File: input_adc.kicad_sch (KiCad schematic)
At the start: 8 parts

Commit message: Init Documentación
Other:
- note added: "Etapa: Entradas analógias"
- note added: "Pines ESP32/Input ADC - IA07 - IA08"
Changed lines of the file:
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@@
     (stroke (width 0) (type default) (color 0 0 0 0))
+  )
+  (text "Etapa: Entradas analógias" (at 99.06 45.72 0)
+    (effects (font (size 5.08 5.08) (thickness 1.016) bold) (justify left bottom))
+  )
+  (text "Pines ESP32/Input ADC\n\n- IA07\n- IA08\n\n\n" (at 60.96 157.48 0)
+    (effects (font (size 2.54 2.54)) (justify left bottom))
   )
   (global_label "IA08" (shape input) (at 120.65 105.41 180) (fields_autoplaced)

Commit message: update esq raiz
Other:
- moved on the sheet: C?, R?, U?B

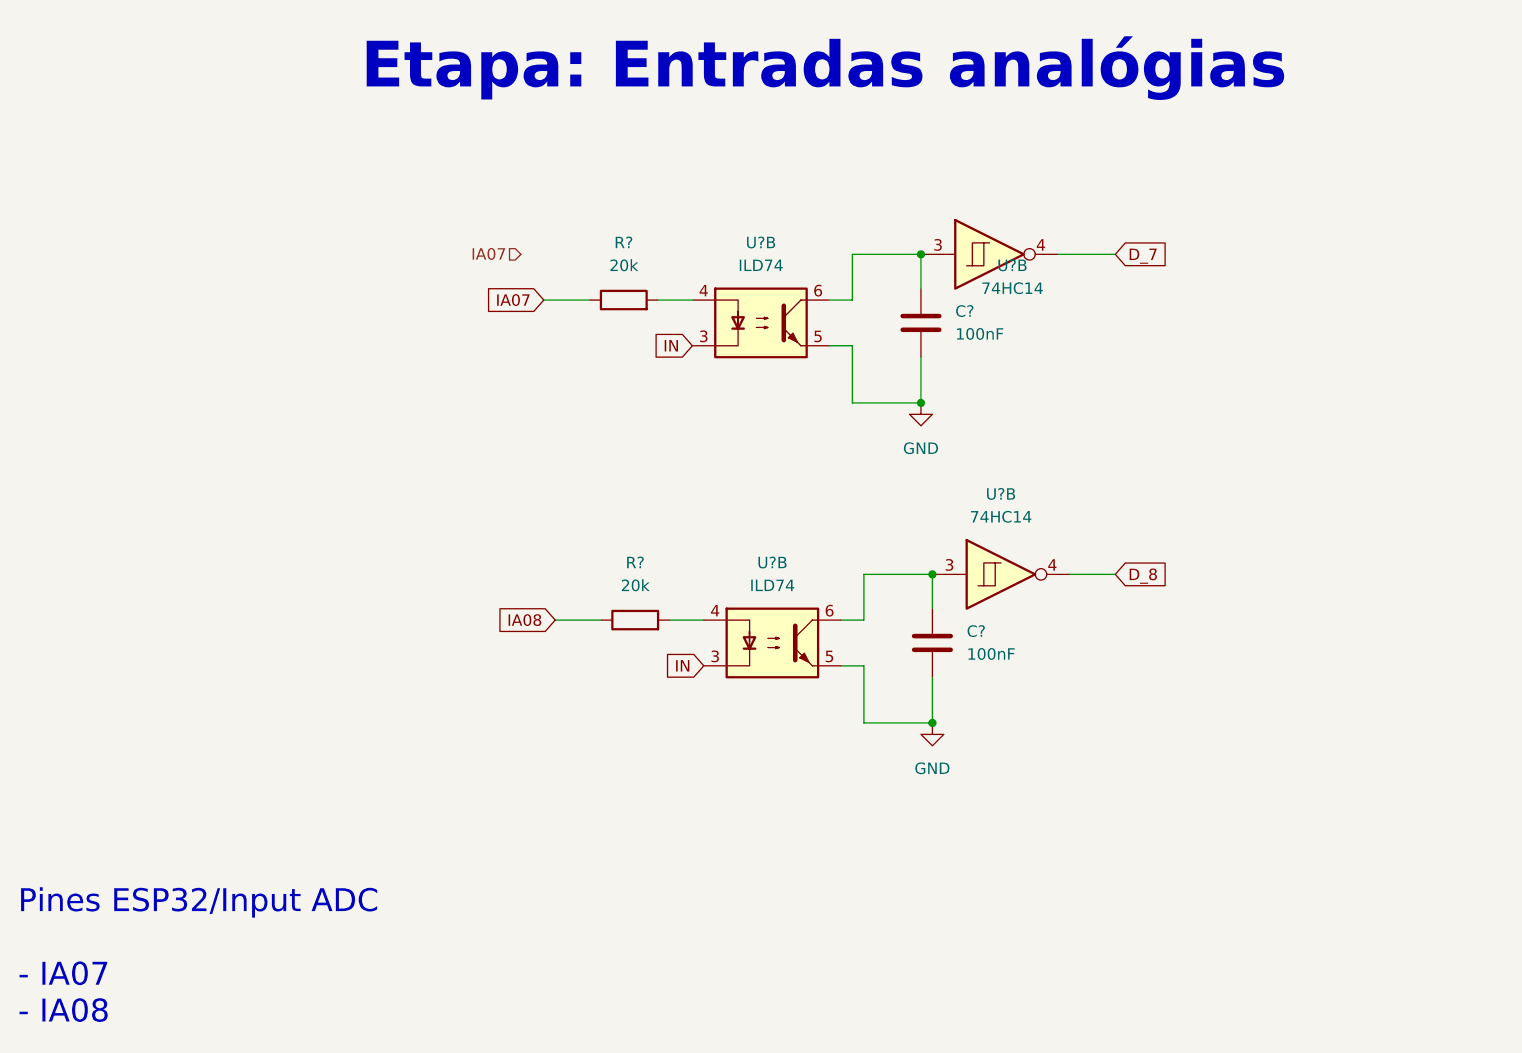
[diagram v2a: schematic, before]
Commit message: add salidas separadas 1,2,3
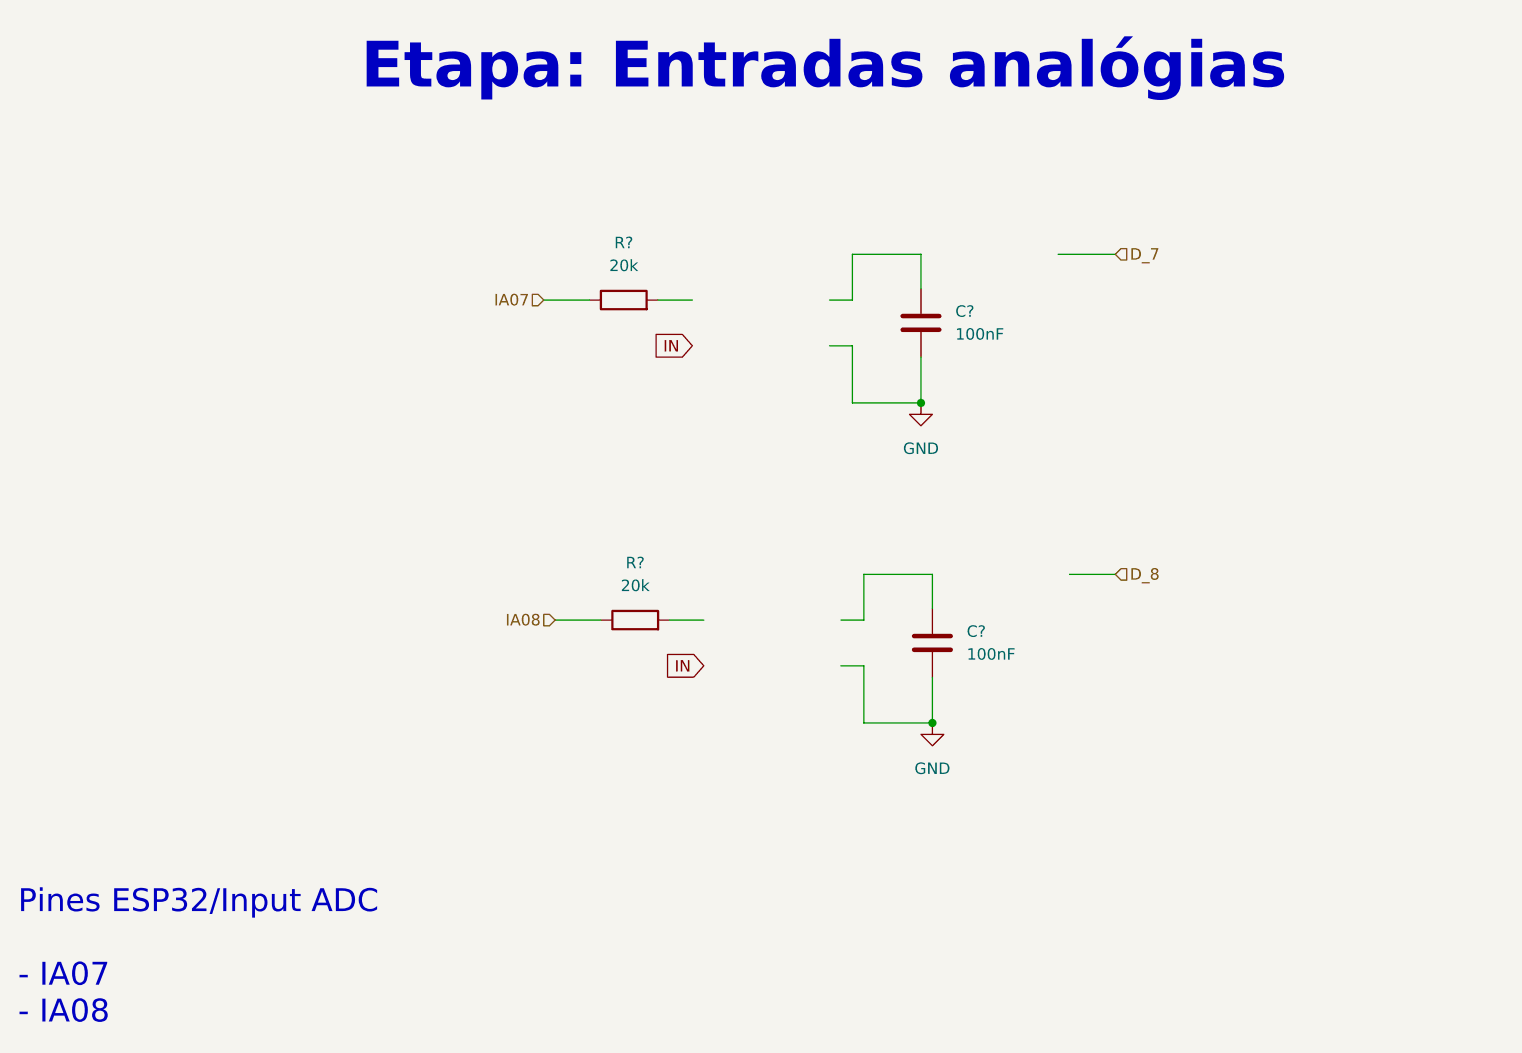
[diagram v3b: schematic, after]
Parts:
- removed U? (x2): ILD74, Package_DIP:DIP-4_W7.62mm, symbol Isolator:ILD74
- removed U? (x2): 74HC14, Package_SO:TSSOP-14_4.4x5mm_P0.65mm, symbol 74xx:74HC14
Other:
- company: (none) -> INTEAMBI
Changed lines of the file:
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@@
 (kicad_sch (version 20211123) (generator eeschema)
   (paper "A4")
-  (junction (at 162.56 99.06) (diameter 0) (color 0 0 0 0)
-  )
-  (junction (at 161.29 63.5) (diameter 0) (color 0 0 0 0)
+  (title_block
+    (date "2022-09-15")
+    (rev "José Luis Laica")
+    (company "INTEAMBI")
   )
   (junction (at 161.29 80.01) (diameter 0) (color 0 0 0 0)
@@
     (effects (font (size 2.54 2.54)) (justify left bottom))
   )
-  (global_label "IA08" (shape input) (at 120.65 104.14 180) (fields_autoplaced)
-    (effects (font (size 1.27 1.27)) (justify right))
-    (property "Intersheet References" "${INTERSHEET_REFS}" (id 0) (at 114.1245 104.0606 0)
-      (effects (font (size 1.27 1.27)) (justify right) hide)
-    )
-  )
-  (global_label "D_8" (shape input) (at 182.88 99.06 0) (fields_autoplaced)
-    (effects (font (size 1.27 1.27)) (justify left))
-    (property "Intersheet References" "${INTERSHEET_REFS}" (id 0) (at 188.7402 98.9806 0)
-      (effects (font (size 1.27 1.27)) (justify left) hide)
-    )
-  )
   (global_label "IN" (shape input) (at 135.89 73.66 180) (fields_autoplaced)
     (effects (font (size 1.27 1.27)) (justify right))
@@
     )
   )
-  (global_label "IA07" (shape input) (at 119.38 68.58 180) (fields_autoplaced)
+  (hierarchical_label "D_7" (shape input) (at 182.88 63.5 0)
+    (effects (font (size 1.27 1.27)) (justify left))
+  )
+  (hierarchical_label "IA07" (shape input) (at 119.38 68.58 180)
     (effects (font (size 1.27 1.27)) (justify right))
-    (property "Intersheet References" "${INTERSHEET_REFS}" (id 0) (at 112.8545 68.5006 0)
-      (effects (font (size 1.27 1.27)) (justify right) hide)
-    )
   )
-  (global_label "D_7" (shape input) (at 182.88 63.5 0) (fields_autoplaced)
+  (hierarchical_label "D_8" (shape input) (at 182.88 99.06 0)
     (effects (font (size 1.27 1.27)) (justify left))
-    (property "Intersheet References" "${INTERSHEET_REFS}" (id 0) (at 188.7402 63.4206 0)
-      (effects (font (size 1.27 1.27)) (justify left) hide)
-    )
   )
-  (hierarchical_label "IA07" (shape input) (at 116.84 63.5 180)
+  (hierarchical_label "IA08" (shape input) (at 120.65 104.14 180)
     (effects (font (size 1.27 1.27)) (justify right))
   )
   (symbol (lib_id "power:GND") (at 161.29 80.01 0) (unit 1)
     (in_bom yes) (on_board yes) (fields_autoplaced)
-    (property "Reference" "#PWR?" (id 0) (at 161.29 86.36 0)
+    (property "Reference" "#PWR0117" (id 0) (at 161.29 86.36 0)
       (effects (font (size 1.27 1.27)) hide)
     )
@@
     )
     (pin "1")
-  )
-  (symbol (lib_id "Isolator:ILD74") (at 143.51 71.12 0) (unit 2)
-    (in_bom yes) (on_board yes) (fields_autoplaced)
-    (property "Reference" "U?" (id 0) (at 143.51 62.23 0))
-    (property "Value" "ILD74" (id 1) (at 143.51 64.77 0))
-    (property "Footprint" "Package_DIP:DIP-4_W7.62mm" (id 2) (at 138.43 76.2 0)
-      (effects (font (size 1.27 1.27) italic) (justify left) hide)
-    )
-    (property "Datasheet" "https://www.vishay.com/docs/83640/ild74.pdf" (id 3) (at 143.51 71.12 0)
-      (effects (font (size 1.27 1.27)) (justify left) hide)
-    )
-    (pin "1")
-    (pin "2")
-    (pin "7")
-    (pin "8")
-    (pin "3")
-    (pin "4")
-    (pin "5")
-    (pin "6")
   )
   (symbol (lib_id "Device:R") (at 128.27 68.58 90) (unit 1)
@@
   (symbol (lib_id "power:GND") (at 162.56 115.57 0) (unit 1)
     (in_bom yes) (on_board yes) (fields_autoplaced)
-    (property "Reference" "#PWR?" (id 0) (at 162.56 121.92 0)
+    (property "Reference" "#PWR0118" (id 0) (at 162.56 121.92 0)
       (effects (font (size 1.27 1.27)) hide)
     )
@@
     (pin "2")
   )
-  (symbol (lib_id "Isolator:ILD74") (at 144.78 106.68 0) (unit 2)
-    (in_bom yes) (on_board yes) (fields_autoplaced)
-    (property "Reference" "U?" (id 0) (at 144.78 97.79 0))
-    (property "Value" "ILD74" (id 1) (at 144.78 100.33 0))
-    (property "Footprint" "Package_DIP:DIP-4_W7.62mm" (id 2) (at 139.7 111.76 0)
-      (effects (font (size 1.27 1.27) italic) (justify left) hide)
-    )
-    (property "Datasheet" "https://www.vishay.com/docs/83640/ild74.pdf" (id 3) (at 144.78 106.68 0)
-      (effects (font (size 1.27 1.27)) (justify left) hide)
-    )
-    (pin "1")
-    (pin "2")
-    (pin "7")
-    (pin "8")
-    (pin "3")
-    (pin "4")
-    (pin "5")
-    (pin "6")
-  )
-  (symbol (lib_id "74xx:74HC14") (at 170.18 99.06 0) (unit 2)
-    (in_bom yes) (on_board yes) (fields_autoplaced)
-    (property "Reference" "U?" (id 0) (at 170.18 90.17 0))
-    (property "Value" "74HC14" (id 1) (at 170.18 92.71 0))
-    (property "Footprint" "Package_SO:TSSOP-14_4.4x5mm_P0.65mm" (id 2) (at 170.18 99.06 0)
-      (effects (font (size 1.27 1.27)) hide)
-    )
-    (property "Datasheet" "http://www.ti.com/lit/gpn/sn74HC14" (id 3) (at 170.18 99.06 0)
-      (effects (font (size 1.27 1.27)) hide)
-    )
-    (pin "1")
-    (pin "2")
-    (pin "3")
-    (pin "4")
-    (pin "5")
-    (pin "6")
-    (pin "8")
-    (pin "9")
-    (pin "10")
-    (pin "11")
-    (pin "12")
-    (pin "13")
-    (pin "14")
-    (pin "7")
-  )
-  (symbol (lib_id "74xx:74HC14") (at 168.91 63.5 0) (unit 2)
-    (in_bom yes) (on_board yes)
-    (property "Reference" "U?" (id 0) (at 171.45 64.77 0))
-    (property "Value" "74HC14" (id 1) (at 171.45 67.31 0))
-    (property "Footprint" "Package_SO:TSSOP-14_4.4x5mm_P0.65mm" (id 2) (at 168.91 63.5 0)
-      (effects (font (size 1.27 1.27)) hide)
-    )
-    (property "Datasheet" "http://www.ti.com/lit/gpn/sn74HC14" (id 3) (at 168.91 63.5 0)
-      (effects (font (size 1.27 1.27)) hide)
-    )
-    (pin "1")
-    (pin "2")
-    (pin "3")
-    (pin "4")
-    (pin "5")
-    (pin "6")
-    (pin "8")
-    (pin "9")
-    (pin "10")
-    (pin "11")
-    (pin "12")
-    (pin "13")
-    (pin "14")
-    (pin "7")
-  )
   (symbol (lib_id "Device:C") (at 161.29 71.12 0) (unit 1)
